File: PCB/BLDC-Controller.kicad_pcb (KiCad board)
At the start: 2 copper layers, 104 parts, among them J1 Prog, J2 Receiver, J3 ICSP, Q1 IRFZ44N, Q2 IRFZ44N, Q3 IRFZ44N, Q4 IRFZ44N, Q5 IRFZ44N, Q6 IRFZ44N, SW1 RST, SW2 Speed+, SW3 Speed-, U1 UCC27211ADRM, U2 UCC27211ADRM, U3 UCC27211ADRM, U4 ATmega328P-P, U5 LM317, U6 LM7805, Y1 16M

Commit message: 28/10/2023 update
Began initial PCB layout.
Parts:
- removed the C11 at (150.4, 110.0)
- removed the C14 at (125.9, 40.5)
- removed C22: 100n, Capacitor_THT:C_Disc_D6.0mm_W2.5mm_P5.00mm
- removed C23, C24, C26: 1n, Capacitor_THT:C_Disc_D6.0mm_W2.5mm_P5.00mm
- removed C25: 22p, Capacitor_THT:C_Disc_D6.0mm_W2.5mm_P5.00mm
- removed J3: ICSP, Connector_PinSocket_2.54mm:PinSocket_2x03_P2.54mm_Vertical
- C1, C16, C17: footprint Capacitor_THT:C_Disc_D6.0mm_W2.5mm_P5.00mm -> Ariamelon-Device:CP_Radial_D5.0mm_P2.54mm
- C10: value 1u -> 10u; footprint Capacitor_THT:C_Disc_D6.0mm_W2.5mm_P5.00mm -> Ariamelon-Device:CP_Radial_D5.0mm_P2.54mm
- C11: renamed from C15; footprint Capacitor_THT:C_Disc_D6.0mm_W2.5mm_P5.00mm -> Ariamelon-Device:CP_Radial_D5.0mm_P2.54mm
- C12, C4, C7: value 1000u -> 10u; footprint Capacitor_THT:CP_Radial_D16.0mm_P7.50mm -> Ariamelon-Device:CP_Radial_D5.0mm_P2.54mm
- C13, C3: footprint Capacitor_THT:CP_Radial_D16.0mm_P7.50mm -> Ariamelon-Device:CP_Radial_D16.0mm_P7.62mm
- C14: renamed from C27; footprint Capacitor_THT:C_Disc_D5.0mm_W2.5mm_P2.50mm -> Ariamelon-Device:C_Disc_D5.0mm_W2.5mm_P2.54mm
- C15: renamed from C28; footprint Capacitor_THT:C_Disc_D5.0mm_W2.5mm_P2.50mm -> Ariamelon-Device:C_Disc_D5.0mm_W2.5mm_P2.54mm
- C18, C19: value 10u -> 100n; footprint Capacitor_THT:C_Disc_D6.0mm_W2.5mm_P5.00mm -> Ariamelon-Device:C_Disc_D6.0mm_W2.5mm_P5.08mm
- C2: value 1u -> 680n; footprint Capacitor_THT:C_Disc_D6.0mm_W2.5mm_P5.00mm -> Ariamelon-Device:C_Rect_L7.0mm_W4.5mm_P5.08mm
- C20: footprint Capacitor_THT:C_Disc_D6.0mm_W2.5mm_P5.00mm -> Ariamelon-Device:C_Disc_D6.0mm_W2.5mm_P5.08mm
- C21: value 100n -> 22p; footprint Capacitor_THT:C_Disc_D6.0mm_W2.5mm_P5.00mm -> Ariamelon-Device:C_Disc_D5.0mm_W2.5mm_P2.54mm
- C5: value 10u -> 680n; footprint Capacitor_THT:C_Disc_D6.0mm_W2.5mm_P5.00mm -> Ariamelon-Device:C_Rect_L7.0mm_W4.5mm_P5.08mm
- C6: value 1u -> 1000u; footprint Capacitor_THT:C_Disc_D6.0mm_W2.5mm_P5.00mm -> Ariamelon-Device:CP_Radial_D16.0mm_P7.62mm
- C8: value 1000u -> 680n; footprint Capacitor_THT:CP_Radial_D16.0mm_P7.50mm -> Ariamelon-Device:C_Rect_L7.0mm_W4.5mm_P5.08mm
- C9: value 10u -> 1000u; footprint Capacitor_THT:C_Disc_D6.0mm_W2.5mm_P5.00mm -> Ariamelon-Device:CP_Radial_D16.0mm_P7.62mm
- D10, D11, D12, D15, D16, D17, D18, D19, D20, D21, D3, D4, D5, D6, D9: footprint Diode_THT:D_DO-41_SOD81_P7.62mm_Horizontal -> Diode_THT:D_DO-35_SOD27_P7.62mm_Horizontal
- Q1, Q2, Q3, Q4, Q5, Q6: value IRFZ44N -> P75NF75
- R1, R15, R24, R8: value 10 -> 1; footprint Resistor_THT:R_Axial_DIN0207_L6.3mm_D2.5mm_P7.62mm_Horizontal -> Resistor_THT:R_Axial_DIN0204_L3.6mm_D1.6mm_P7.62mm_Horizontal
- R10, R11, R12, R13, R14, R16, R17, R18, R19, R2, R20, R21, R22, R23, R25, R26, R27, R28, R29, R3, R30, R31, R32, R33, R34, R35, R36, R4, R5, R6, R7, R9: footprint Resistor_THT:R_Axial_DIN0207_L6.3mm_D2.5mm_P7.62mm_Horizontal -> Resistor_THT:R_Axial_DIN0204_L3.6mm_D1.6mm_P7.62mm_Horizontal
- U1, U2, U3: value UCC27211ADRM -> UCC27282; footprint Ariamelon-Package:SOIC-8_3.9x4.9mm_P1.27mm -> Package_DIP:DIP-8_W7.62mm_Socket
- U4: footprint Package_DIP:DIP-28_W7.62mm -> Package_DIP:DIP-28_W7.62mm_Socket
- Y1: footprint Crystal:Crystal_HC49-U_Vertical -> Crystal:Crystal_HC49-4H_Vertical
- moved C10 149.3 mm to (48.3, 58.4)
- moved C21 146.2 mm to (34.3, 147.3), turned to 90 degrees
- moved SW2 130.8 mm to (58.6, 149.3), turned to 90 degrees
- moved C2 121.2 mm to (66.0, 63.5)
- moved C11 118.7 mm to (38.1, 124.5), turned to -90 degrees
- moved D21 116.9 mm to (27.9, 88.9), turned to 180 degrees
- moved C17 116.5 mm to (15.2, 88.9), turned to -90 degrees
- moved SW3 115.3 mm to (58.7, 136.6), turned to 90 degrees
- moved C15 112.4 mm to (34.3, 140.7), turned to 90 degrees
- moved Y1 111.5 mm to (38.6, 134.2), turned to -90 degrees
- moved C12 111.4 mm to (55.9, 68.6)
- moved SW1 111.1 mm to (52.8, 105.8), turned to 180 degrees
- moved C1 110.8 mm to (76.2, 63.5), turned to 90 degrees
- moved R1 110.8 mm to (66.0, 58.4)
- moved C14 110.7 mm to (34.3, 132.0), turned to -90 degrees
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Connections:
- C1 pad 1: GND -> Net-(U1-VDD)
- C1 pad 2: Net-(U1-VDD) -> GND
- C10 pad 1: /MCU/Phase_Out_C -> VCC
- C10 pad 2: Net-(U3-HB) -> GND
- C11 pad 1: GND -> +5V
- C11 pad 2: +5V -> GND
- C12 pad 1: VCC -> Net-(D20-A)
- C13 pad 1: VCC -> +12V
- C16 pad 1: GND -> Net-(D21-K)
- C16 pad 2: +12V -> GND
- C17 pad 1: GND -> +5V
- C17 pad 2: +12V -> GND
- C18 pad 1: GND -> RST
- C18 pad 2: Net-(D21-K) -> GND
- C19 pad 1: GND -> Speed+
- C19 pad 2: +5V -> GND
- C20 pad 1: RST -> Speed-
- C21 pad 1: Speed+ -> GND
- C21 pad 2: GND -> PWM_In
- C4 pad 1: VCC -> Net-(U2-VDD)
- C5 pad 1: GND -> /MCU/Phase_Out_B
- C5 pad 2: Net-(U2-VDD) -> Net-(U2-HB)
- C6 pad 1: /MCU/Phase_Out_B -> VCC
- C6 pad 2: Net-(U2-HB) -> GND
- C7 pad 1: VCC -> Net-(U3-VDD)
- C8 pad 1: VCC -> /MCU/Phase_Out_C
- C8 pad 2: GND -> Net-(U3-HB)
- C9 pad 1: GND -> VCC
- C9 pad 2: Net-(U3-VDD) -> GND
- D20 pad 2: +12V -> Net-(D20-A)
- J1 pad 2: TX -> RX
- J1 pad 3: RX -> TX
- R22 pad 2: Net-(U5-ADJ) -> Net-(D20-A)
- R23 pad 2: Net-(U5-ADJ) -> Net-(D20-A)
- R30 pad 1: V_Sen_A -> V_Sen_C
- R33 pad 2: V_Sen_A -> V_Sen_C
- R36 pad 2: V_Sen_A -> V_Sen_C
- U1 pad 5: RX -> /MCU/HI_A
- U3 pad 5: /MCU/HI_C -> RX
- U4 pad 17: MOSI -> unconnected-(U4-PB3-Pad17)
- U4 pad 18: MISO -> unconnected-(U4-PB4-Pad18)
- U4 pad 19: SCK -> unconnected-(U4-PB5-Pad19)
- U4 pad 23: V_Sen_A -> V_Sen_C
- U4 pad 26: /MCU/LI_A -> /MCU/LI_C
- U4 pad 28: /MCU/LI_C -> /MCU/LI_A
- U4 pad 4: /MCU/HI_C -> /MCU/HI_A
- U5 pad 1: Net-(U5-ADJ) -> Net-(D20-A)
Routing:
- net +5V: track 0.00 -> 84.5 mm
- net GND: track 0.00 -> 57.8 mm
- net /MCU/Phase_Out_C: track 0.00 -> 47.4 mm
- net /MCU/Phase_Out_A: track 0.00 -> 47.4 mm
- net /MCU/Phase_Out_B: track 0.00 -> 47.4 mm
- net VCC: track 0.00 -> 27.9 mm
- net +12V: track 0.00 -> 26.7 mm
- net Speed-: track 0.00 -> 22.7 mm
- net Net-(D13-K): track 0.00 -> 21.4 mm
- net Net-(D1-K): track 0.00 -> 21.4 mm
- net Net-(D7-K): track 0.00 -> 21.4 mm
- net Net-(D20-A): track 0.00 -> 20.3 mm
- net Speed+: track 0.00 -> 19.5 mm
- net Net-(D4-K): track 0.00 -> 15.2 mm
- net Net-(D15-K): track 0.00 -> 15.2 mm
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- added copper zone on B.Cu, net /MCU/Phase_Out_A
- added copper zone on B.Cu, net /MCU/Phase_Out_B
- added copper zone on B.Cu, net /MCU/Phase_Out_C

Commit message: 30/10/2023 update
Completed initial PCB layout.
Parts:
- removed the C19 at (58.4, 139.7)
- removed the C20 at (58.4, 127.0)
- removed the C3 at (124.5, 91.4)
- removed the C6 at (142.2, 91.4)
- removed the R26 at (55.9, 147.3)
- removed the R27 at (55.9, 134.6)
- added C12: 10u, Ariamelon-Device:CP_Radial_D5.0mm_P2.54mm, F.Cu at (142.7, 70.8)
- added C7: 1000u, Ariamelon-Device:CP_Radial_D16.0mm_P7.62mm, F.Cu at (61.0, 40.1)
- added C8: 1000u, Ariamelon-Device:CP_Radial_D16.0mm_P7.62mm, F.Cu at (61.0, 57.6)
- added H1: VCC, Ariamelon-HolePad:MountingHole_3.2mm_M3_Pad, F.Cu at (58.7, 24.6)
- added J3: Bat_In, Connector_AMASS:AMASS_XT60-M_1x02_P7.20mm_Vertical, F.Cu at (68.4, 88.6)
- moved J2 139.4 mm to (163.1, 88.1), turned to -90 degrees
- moved C20 137.9 mm to (160.5, 91.9), turned to 180 degrees
- moved SW2 130.0 mm to (163.2, 72.1), turned to 180 degrees
- moved C15 129.2 mm to (153.9, 91.9), turned to 180 degrees
- moved R19 128.8 mm to (165.1, 44.9), turned to 180 degrees
- moved R31 120.9 mm to (160.0, 55.1), turned to -90 degrees
- moved D18 119.7 mm to (157.5, 37.3), turned to 0 degrees
- moved D16 119.1 mm to (157.5, 39.8), turned to 0 degrees
- moved R21 118.5 mm to (157.5, 42.4), turned to 0 degrees
- moved Y1 118.4 mm to (147.4, 87.6), turned to 0 degrees
- moved C13 118.0 mm to (145.2, 91.9), turned to 0 degrees
- moved R28 117.9 mm to (157.5, 62.7), turned to 180 degrees
- moved Q6 117.9 mm to (154.9, 32.2), turned to 0 degrees
- moved D14 117.7 mm to (157.5, 47.5), turned to 0 degrees
- moved SW3 114.8 mm to (153.6, 72.1), turned to 180 degrees
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- renumbered C11 to C10, C10 to C11, C14 to C13, C12 to C14, C13 to C16, C18 to C17, C16 to C18, C17 to C19, C21 to C20, C4 to C3, C5 to C4, C7 to C5, C8 to C6, R28 to R26, R29 to R27, R30 to R28, R31 to R29, R32 to R30, R33 to R31, R34 to R32, R35 to R33, R36 to R34
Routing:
- net GND: track 57.8 -> 475.0 mm, vias 0 -> 9
- net +12V: track 26.7 -> 118.6 mm, vias 0 -> 1
- net RX: track 5.08 -> 82.8 mm, vias 0 -> 2
- net /MCU/HI_A: track 0.00 -> 75.1 mm, vias 0 -> 2
- net TX: track 5.08 -> 66.7 mm, vias 0 -> 2
- net V_Sen_COM: track 0.00 -> 61.6 mm, vias 0 -> 1
- net +5V: track 84.5 -> 131.1 mm
- net /MCU/LI_C: track 0.00 -> 44.6 mm
- net /MCU/LI_A: track 0.00 -> 37.1 mm
- net V_Sen_A: track 6.13 -> 42.8 mm, vias 0 -> 1
- net V_Sen_C: track 3.59 -> 31.2 mm, vias 0 -> 1
- net VCC: track 27.9 -> 50.8 mm
- net /MCU/LI_B: track 0.00 -> 21.6 mm
- net V_Sen_B: track 3.59 -> 22.3 mm, vias 0 -> 1
- net Speed-: track 22.7 -> 4.06 mm
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- added copper zone on B.Cu, net GND
- added copper zone on B.Cu, net VCC
- added copper zone on F.Cu, net VCC
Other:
- board outline added: 114.3 x 76.5 mm
- board text added: "400x"

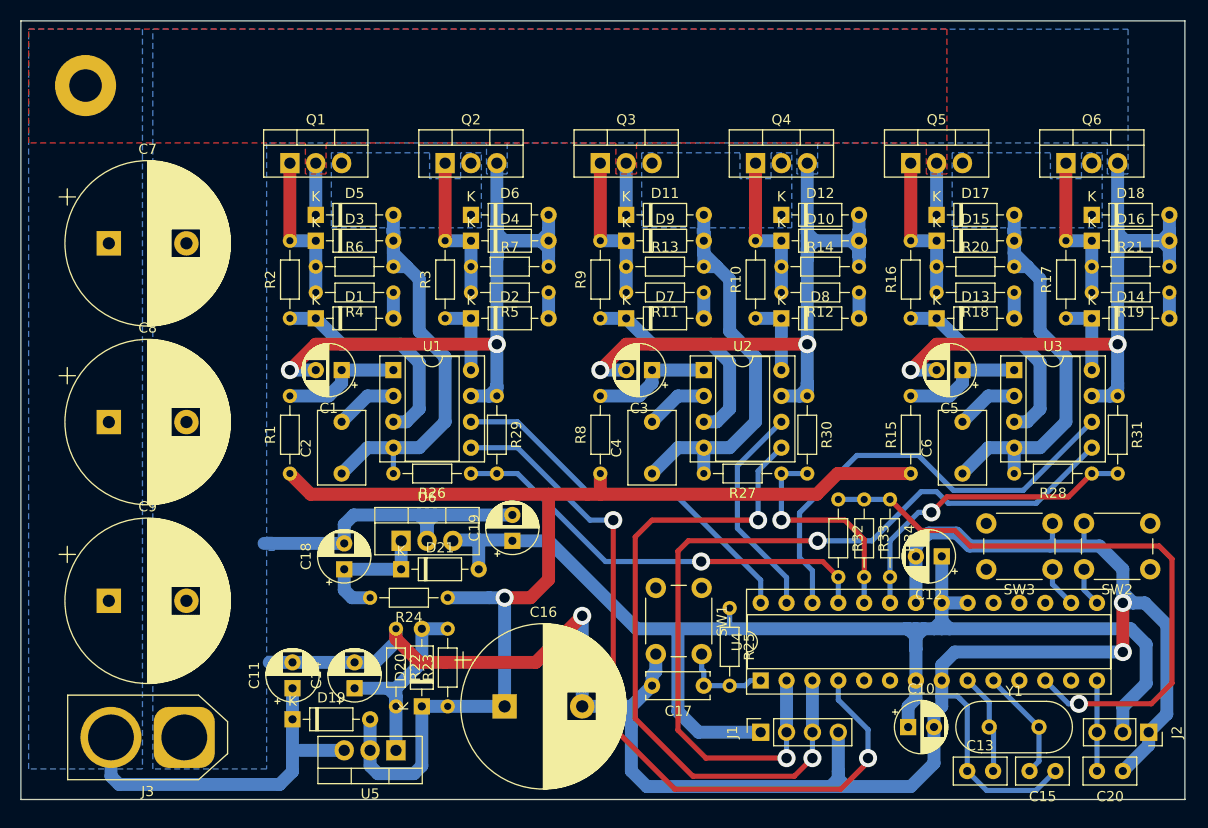
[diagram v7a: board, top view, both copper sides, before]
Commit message: Fixed pin assignment. Added tentative arduino code.
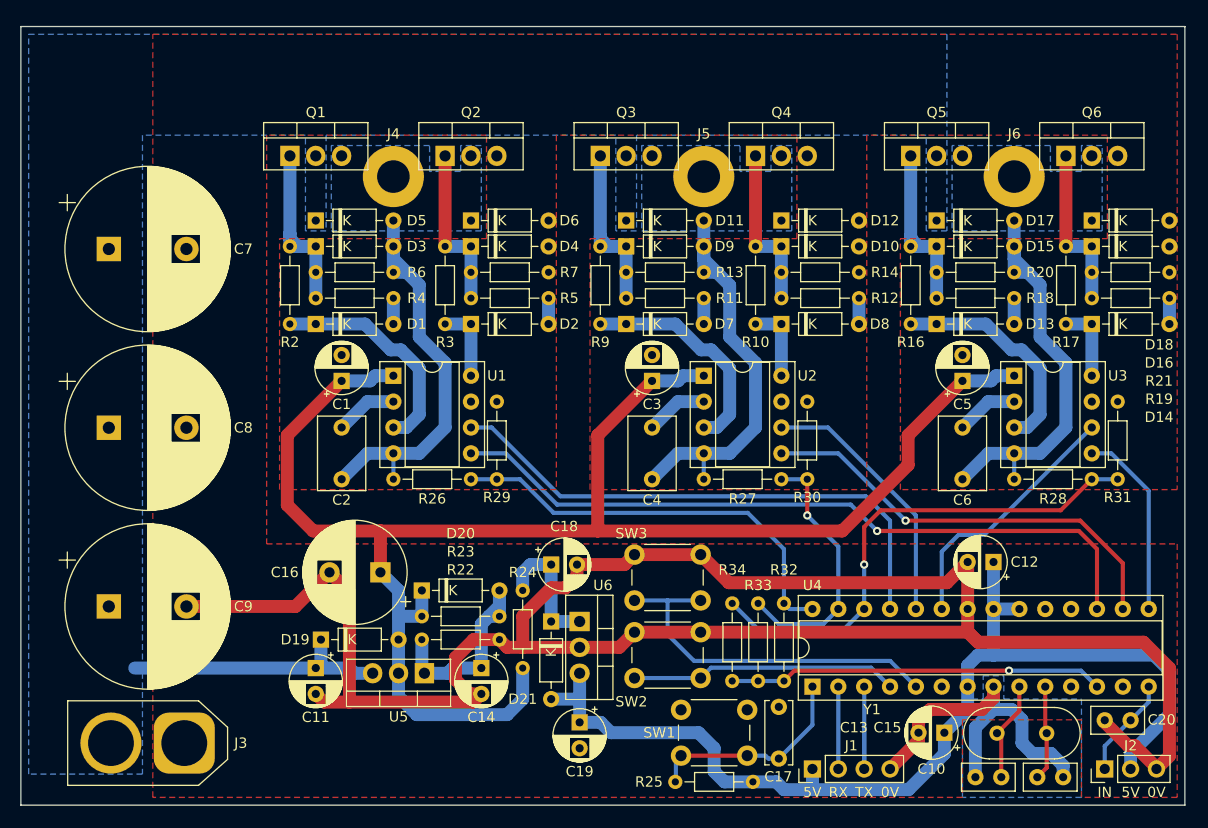
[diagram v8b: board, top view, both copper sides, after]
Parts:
- removed H1: VCC, Ariamelon-HolePad:MountingHole_3.2mm_M3_Pad
- removed R1, R15, R8: 1, Resistor_THT:R_Axial_DIN0204_L3.6mm_D1.6mm_P7.62mm_Horizontal
- added A1: Art, Ariamelon-Logo:Ariamelon_Logo_Large_Mask, F.Cu at (81.3, 23.4)
- added J4: Mot_Con, Ariamelon-HolePad:MountingHole_3.2mm_M3_Pad, F.Cu at (88.9, 33.5)
- added J5: Mot_Con, Ariamelon-HolePad:MountingHole_3.2mm_M3_Pad, F.Cu at (119.4, 33.5)
- added J6: Mot_Con, Ariamelon-HolePad:MountingHole_3.2mm_M3_Pad, F.Cu at (149.9, 33.5)
- C16: value 1000u -> 470u; footprint Ariamelon-Device:CP_Radial_D16.0mm_P7.62mm -> Capacitor_THT:CP_Radial_D10.0mm_P5.00mm
- J1: footprint Connector_PinSocket_2.54mm:PinSocket_1x04_P2.54mm_Vertical -> Connector_PinHeader_2.54mm:PinHeader_1x04_P2.54mm_Vertical
- J2: footprint Connector_PinSocket_2.54mm:PinSocket_1x03_P2.54mm_Vertical -> Connector_PinHeader_2.54mm:PinHeader_1x03_P2.54mm_Vertical
- moved SW2 45.4 mm to (119.1, 82.8)
- moved SW3 34.7 mm to (119.1, 75.1)
- moved R34 23.6 mm to (122.2, 83.1), turned to 90 degrees
- moved R33 20.6 mm to (124.7, 83.1), turned to 90 degrees
- moved C18 20.3 mm to (104.4, 71.6), turned to 0 degrees
- moved U6 19.2 mm to (107.2, 77.2), turned to -90 degrees
- moved C19 19.0 mm to (107.2, 87.1), turned to -90 degrees
- moved R32 18.6 mm to (127.3, 83.1), turned to 90 degrees
- moved C16 17.9 mm to (87.6, 72.4), turned to 180 degrees
- moved R25 17.2 mm to (124.2, 93.0), turned to 180 degrees
- moved SW1 17.1 mm to (123.6, 90.4), turned to 180 degrees
- moved D21 15.6 mm to (104.4, 77.2), turned to -90 degrees
- moved C14 12.6 mm to (97.5, 81.8), turned to -90 degrees
- moved D20 11.4 mm to (91.7, 74.2), turned to 0 degrees
- moved C17 10.3 mm to (126.7, 90.7), turned to 90 degrees
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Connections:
- C1 pad 1: Net-(U1-VDD) -> +12V
- C3 pad 1: Net-(U2-VDD) -> +12V
- C5 pad 1: Net-(U3-VDD) -> +12V
- J2 pad 1: GND -> PWM_In
- J2 pad 3: PWM_In -> GND
- SW2 pad 1: Speed+ -> Speed-
- SW3 pad 1: Speed- -> Speed+
- U1 pad 1: Net-(U1-VDD) -> +12V
- U2 pad 1: Net-(U2-VDD) -> +12V
- U2 pad 5: TX -> /MCU/HI_B
- U3 pad 1: Net-(U3-VDD) -> +12V
- U3 pad 5: RX -> /MCU/HI_C
- U4 pad 15: Speed+ -> /MCU/HI_C
- U4 pad 16: Speed- -> /MCU/HI_B
- U4 pad 17: unconnected-(U4-PB3-Pad17) -> /MCU/HI_A
- U4 pad 23: V_Sen_C -> /MCU/LI_C
- U4 pad 24: V_Sen_B -> /MCU/LI_B
- U4 pad 25: V_Sen_A -> /MCU/LI_A
- U4 pad 26: /MCU/LI_C -> V_Sen_C
- U4 pad 27: /MCU/LI_B -> V_Sen_B
- U4 pad 28: /MCU/LI_A -> V_Sen_A
- U4 pad 4: /MCU/HI_A -> Speed-
- U4 pad 5: unconnected-(U4-PD3-Pad5) -> Speed+
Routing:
- net GND: track 475.0 -> 238.8 mm, vias 9 -> 0
- net RX: track 82.8 -> 8.09 mm, vias 2 -> 0
- net TX: track 66.7 -> 12.1 mm, vias 2 -> 0
- net /MCU/HI_B: track 0.00 -> 42.5 mm, vias 0 -> 1
- net +12V: track 118.6 -> 160.8 mm, vias 1 -> 0
- net Speed+: track 3.83 -> 36.3 mm
- net +5V: track 131.1 -> 105.4 mm
- net V_Sen_COM: track 61.6 -> 36.9 mm
- net VCC: track 50.8 -> 27.2 mm
- net Speed-: track 4.06 -> 26.3 mm
- net /MCU/LI_C: track 44.6 -> 25.4 mm
- net V_Sen_C: track 31.2 -> 50.0 mm
- net /MCU/HI_C: track 0.00 -> 18.7 mm
- net /MCU/LI_A: track 37.1 -> 53.6 mm
- net RST: track 8.99 -> 21.0 mm
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- added copper zone on F.Cu, net GND
- removed copper zone on F.Cu, net VCC
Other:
- board text added: "0V"
- board text added: "5V"
- board text added: "BLDC Motor Controller V1.0"
- board text added: "IN"
- board text added: "RX"
- board text added: "TX"
